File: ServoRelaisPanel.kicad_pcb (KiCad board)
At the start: 2 copper layers, 99.8 x 99.6 mm, 202 parts, among them J1 Conn_01x03_Female, J2 ISCP, J3 Conn_01x02_Female, J4 Conn_01x03_Female, Q1 IRLB8721PBF, Q2 IRLB8721PBF, U1 MEE1-0309, U2 PIC10F320-IP

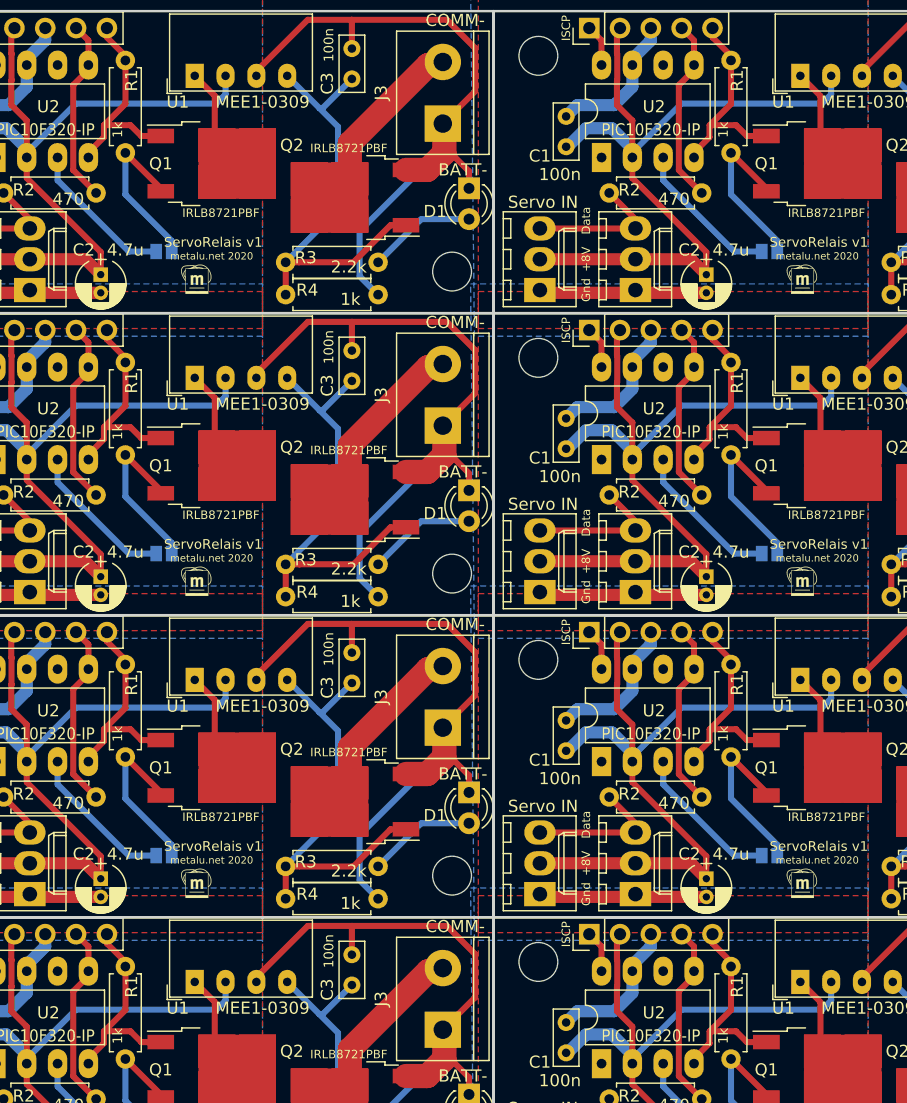
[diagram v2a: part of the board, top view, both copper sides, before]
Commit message: PCB: add solder-switch to disable powering the DC-DC converter (else programming of the PIC fails because of power loss)
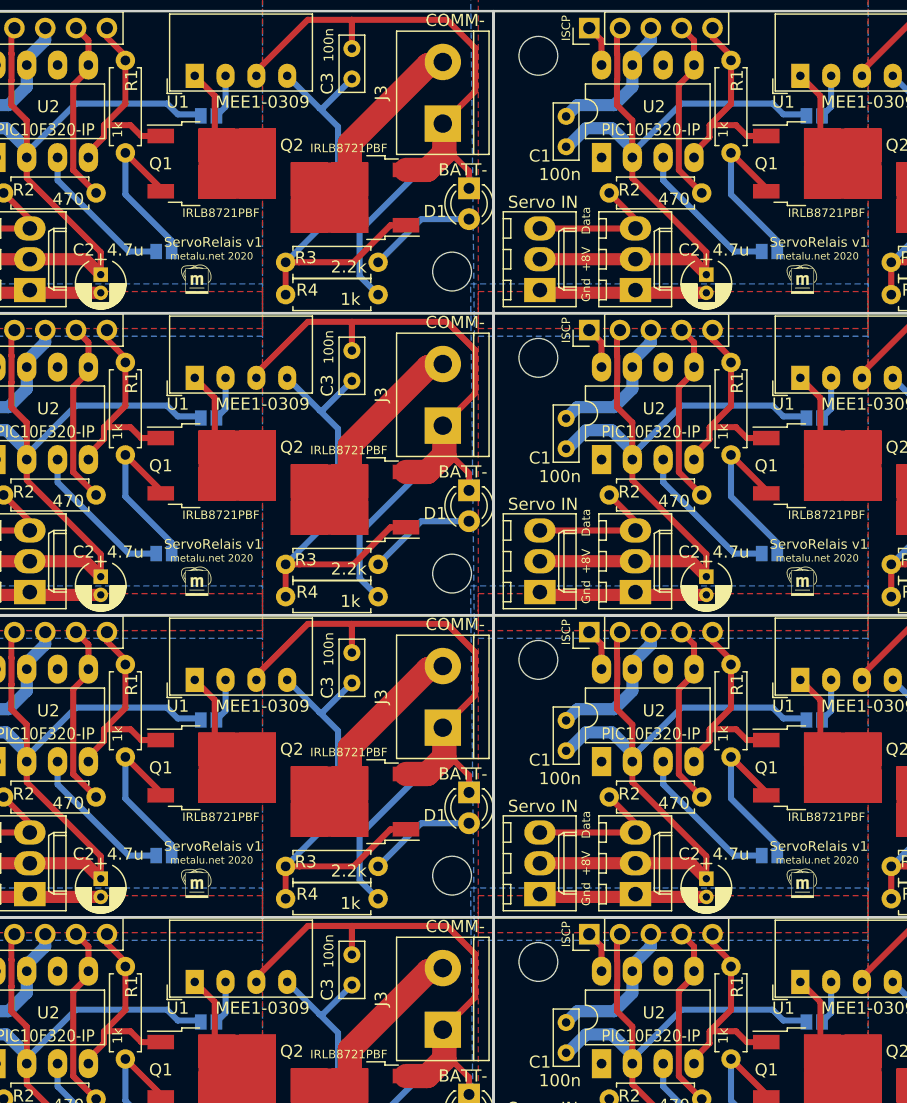
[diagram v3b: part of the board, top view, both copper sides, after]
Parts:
- removed the G*** at (159.1, 127.6)
- removed the G*** at (109.2, 127.6)
- removed the G*** at (159.1, 102.7)
- removed the G*** at (109.2, 102.7)
- removed the G*** at (159.1, 77.9)
- removed the G*** at (109.2, 77.9)
- removed the G*** at (159.1, 53.0)
- added ?: , , F.Cu at (103.9, 143.9)
- added ?: , , F.Cu at (54.0, 143.9)
- added G***: LOGO, metalunet:metalunet, B.Cu at (162.3, 127.4)
- added G***: LOGO, metalunet:metalunet, B.Cu at (112.4, 127.4)
- added G***: LOGO, metalunet:metalunet, B.Cu at (162.3, 102.5)
- added G***: LOGO, metalunet:metalunet, B.Cu at (112.4, 102.5)
- added G***: LOGO, metalunet:metalunet, B.Cu at (162.3, 77.6)
- added G***: LOGO, metalunet:metalunet, B.Cu at (112.4, 77.6)
- added G***: LOGO, metalunet:metalunet, B.Cu at (162.3, 52.7)
- added JP2: (prog), Connect:GS2, B.Cu at (152.7, 123.2)
- added JP2: (prog), Connect:GS2, B.Cu at (102.7, 123.2)
- added JP2: (prog), Connect:GS2, B.Cu at (152.7, 98.3)
- added JP2: (prog), Connect:GS2, B.Cu at (102.7, 98.3)
- added JP2: (prog), Connect:GS2, B.Cu at (152.7, 73.4)
- added JP2: (prog), Connect:GS2, B.Cu at (102.7, 73.4)
- added JP2: (prog), Connect:GS2, B.Cu at (152.7, 48.5)
- added JP2: (prog), Connect:GS2, B.Cu at (102.7, 48.5)
- moved ? 37.0 mm to (127.9, 141.4)
- moved G*** 3.19 mm to (112.4, 52.7)
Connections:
- U1 pad 2: +3V3 -> Net-(JP2-Pad2) (x8)
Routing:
- net Net-(JP2-Pad2): track 0.00 -> 28.9 mm
- net +3V3: track 523.4 -> 495.3 mm

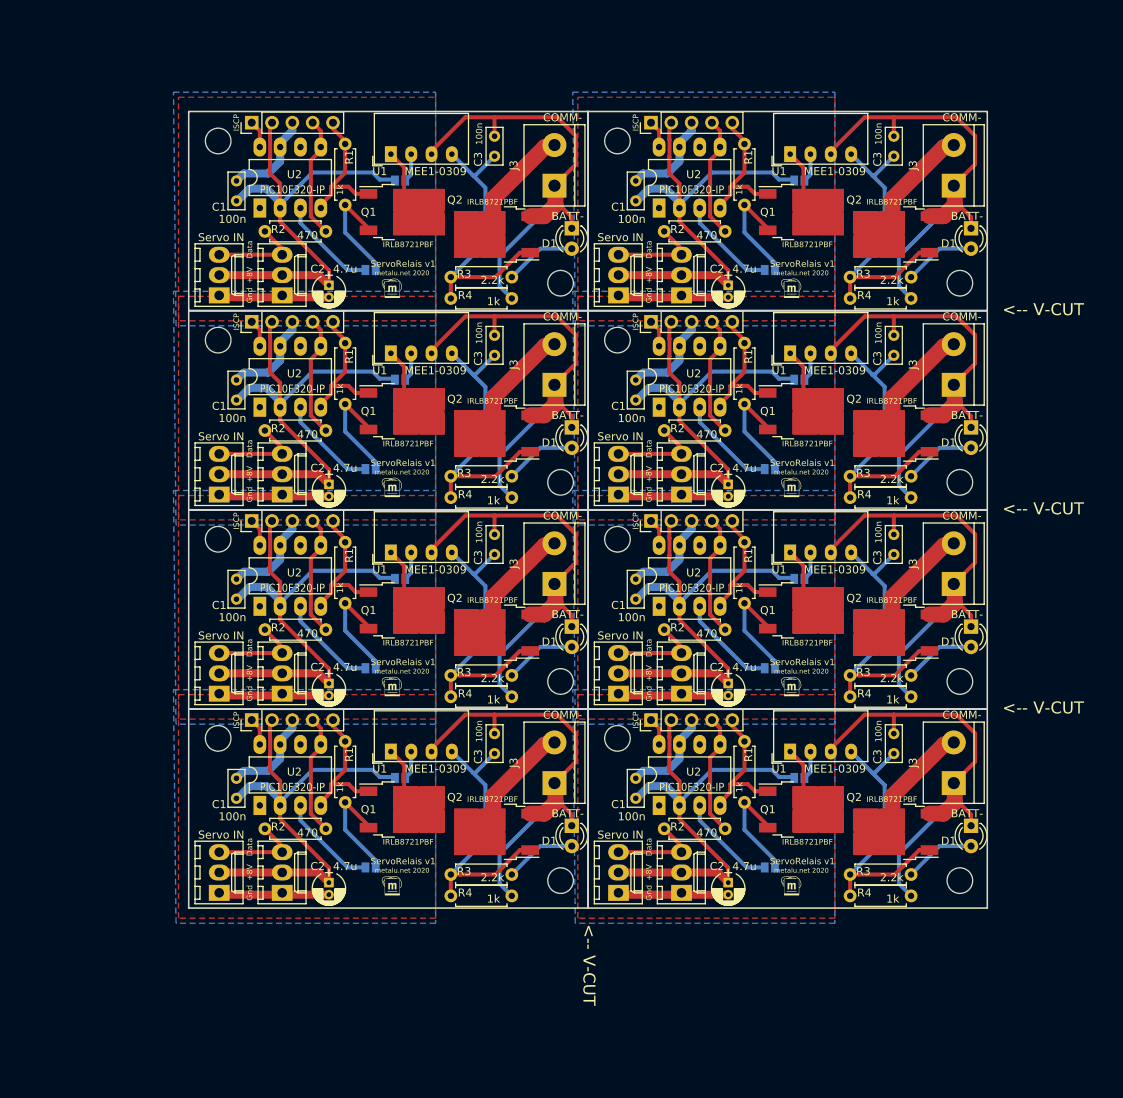
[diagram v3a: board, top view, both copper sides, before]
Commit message: PCB 1.2: add 25Vmax->3V3 regulator
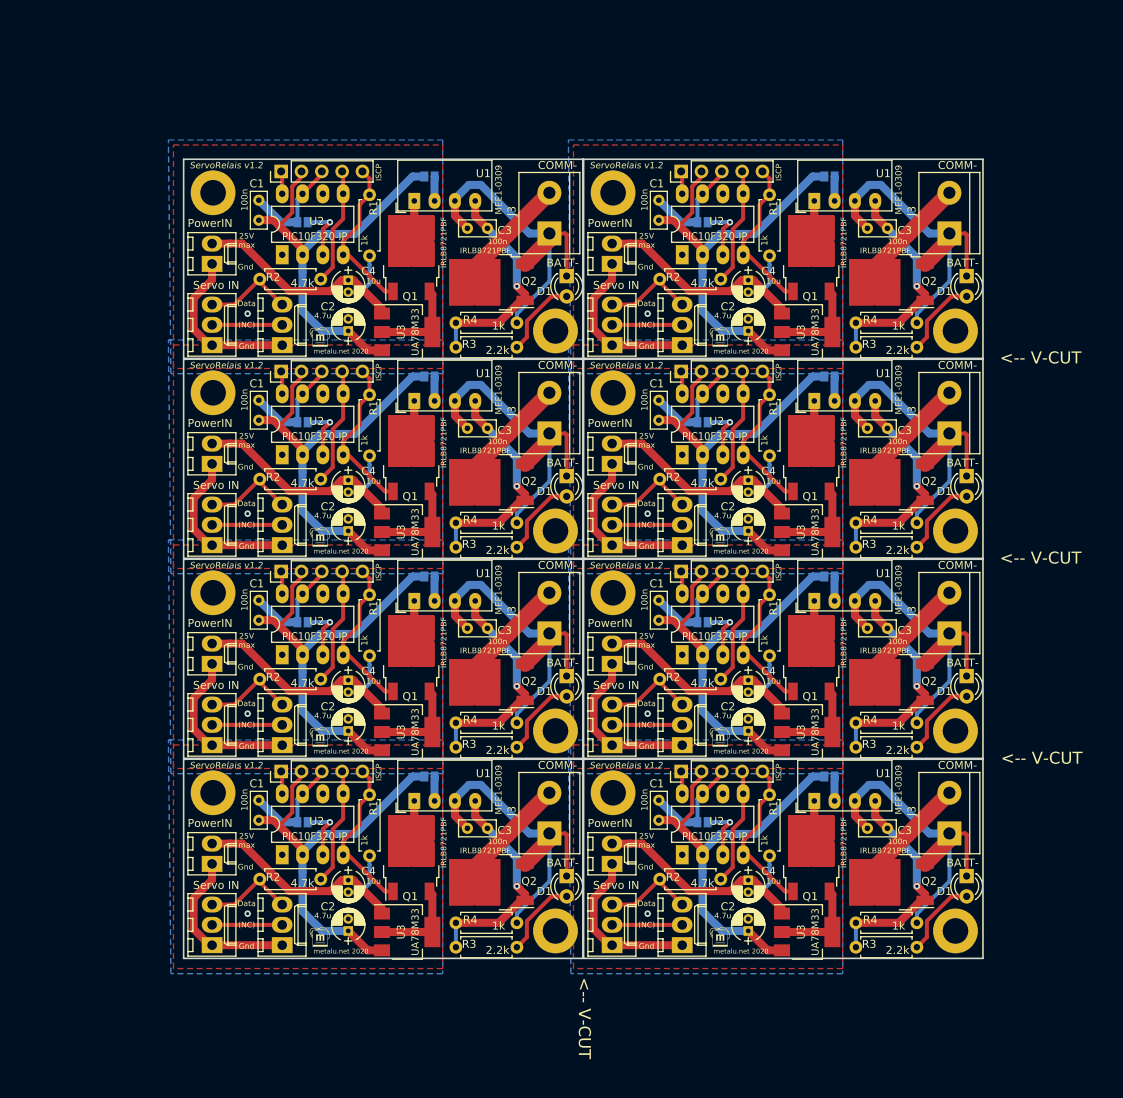
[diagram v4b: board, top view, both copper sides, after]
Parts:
- removed the ? at (139.6, 132.5)
- removed the ? at (140.8, 117.7)
- removed the ? at (90.9, 117.7)
- removed the ? at (140.8, 92.8)
- removed the ? at (90.9, 92.8)
- removed the ? at (140.8, 67.9)
- removed the ? at (140.8, 131.2)
- removed the ? at (90.9, 131.2)
- removed the ? at (140.8, 106.3)
- removed the ? at (90.9, 106.3)
- removed the ? at (140.8, 81.4)
- removed the ? at (89.7, 132.5)
- removed the ? at (90.9, 81.4)
- removed the ? at (140.8, 56.5)
- removed the ? at (139.6, 131.2)
- removed the ? at (89.7, 131.2)
- removed the ? at (139.6, 106.3)
- removed the ? at (89.7, 106.3)
- removed the ? at (139.6, 81.4)
- removed the ? at (89.7, 81.4)
- removed the ? at (139.6, 56.5)
- removed the ? at (140.8, 142.6)
- removed the ? at (139.6, 107.6)
- removed the ? at (127.9, 141.4)
- removed the ? at (90.9, 67.9)
- removed the ? at (89.7, 56.5)
- removed the ? at (90.9, 56.5)
- removed the ? at (89.7, 57.8)
- removed the ? at (89.7, 107.6)
- removed the ? at (139.6, 82.7)
- removed the ? at (89.7, 82.7)
- removed the ? at (139.6, 57.8)
- removed the ? at (103.9, 143.9)
- removed the C1 at (132.2, 125.7)
- removed the C1 at (82.3, 125.7)
- removed the C1 at (132.2, 100.8)
- removed the C1 at (82.3, 100.8)
- removed the C1 at (132.2, 75.9)
- removed the C1 at (82.3, 75.9)
- removed the C1 at (132.2, 51.1)
- removed the C1 at (82.3, 51.1)
- removed the C2 at (143.8, 136.3)
- removed the C2 at (93.9, 136.3)
- removed the C2 at (143.8, 111.4)
- removed the C2 at (93.9, 111.4)
- removed the C2 at (143.8, 86.5)
- removed the C2 at (93.9, 86.5)
- removed the C2 at (143.8, 61.6)
- removed the C3 at (164.5, 120.1)
- removed the C3 at (114.6, 120.1)
- removed the C3 at (164.5, 95.2)
- removed the C3 at (114.6, 95.2)
- removed the C3 at (164.5, 70.4)
- removed the C3 at (114.6, 70.4)
- removed the C3 at (164.5, 45.5)
- removed the C3 at (114.6, 45.5)
- removed the D1 at (174.1, 129.2)
- removed the D1 at (124.2, 129.2)
- removed the D1 at (174.1, 104.3)
- removed the D1 at (124.2, 104.3)
- removed the D1 at (174.1, 79.4)
- removed the D1 at (124.2, 79.4)
- removed the D1 at (174.1, 54.5)
- removed the G*** at (162.3, 127.4)
- removed the G*** at (151.6, 111.8)
- removed the G*** at (101.7, 111.8)
- removed the G*** at (151.6, 86.9)
- removed the G*** at (101.7, 86.9)
- removed the G*** at (151.6, 62.0)
- removed the G*** at (112.4, 127.4)
- removed the G*** at (162.3, 102.5)
- removed the G*** at (112.4, 102.5)
- removed the G*** at (162.3, 77.6)
- removed the G*** at (112.4, 77.6)
- removed the G*** at (162.3, 52.7)
- removed the G*** at (151.6, 136.7)
- removed the G*** at (101.7, 136.7)
- removed the H1 at (129.9, 118.2)
- removed the H1 at (80.0, 118.2)
- removed the H1 at (129.9, 93.3)
- removed the H1 at (80.0, 93.3)
- removed the H1 at (129.9, 68.5)
- removed the H1 at (80.0, 68.5)
- removed the H1 at (129.9, 43.6)
- removed the H2 at (172.7, 136.0)
- removed the H2 at (122.8, 136.0)
- removed the H2 at (172.7, 111.1)
- removed the H2 at (122.8, 111.1)
- removed the H2 at (172.7, 86.2)
- removed the H2 at (122.8, 86.2)
- removed the H2 at (172.7, 61.3)
- removed the J1 at (130.0, 137.5)
- removed the J1 at (80.1, 137.5)
- removed the J1 at (130.0, 112.6)
- removed the J1 at (80.1, 112.6)
- removed the J1 at (130.0, 87.8)
- removed the J1 at (80.1, 87.8)
- removed the J1 at (130.0, 62.9)
- removed the J2 at (134.1, 116.0)
- removed the J2 at (84.2, 116.0)
- removed the J2 at (134.1, 91.1)
- removed the J2 at (84.2, 91.1)
- removed the J2 at (134.1, 66.2)
- removed the J2 at (84.2, 66.2)
- removed the J2 at (134.1, 41.3)
- removed the J3 at (172.0, 123.8)
- removed the J3 at (122.0, 123.8)
- removed the J3 at (172.0, 98.9)
- removed the J3 at (122.0, 98.9)
- removed the J3 at (172.0, 74.0)
- removed the J3 at (122.0, 74.0)
- removed the J3 at (172.0, 49.1)
- removed the J4 at (137.9, 137.5)
- removed the J4 at (88.0, 137.5)
- removed the J4 at (137.9, 112.6)
- removed the J4 at (88.0, 112.6)
- removed the J4 at (137.9, 87.8)
- removed the J4 at (88.0, 87.8)
- removed the J4 at (137.9, 62.9)
- removed the JP1 at (149.0, 134.4)
- removed the JP1 at (99.1, 134.4)
- removed the JP1 at (149.0, 109.5)
- removed the JP1 at (99.1, 109.5)
- removed the JP1 at (149.0, 84.6)
- removed the JP1 at (99.1, 84.6)
- removed the JP1 at (149.0, 59.7)
- removed the JP2 at (152.7, 123.2)
- removed the JP2 at (102.7, 123.2)
- removed the JP2 at (152.7, 98.3)
- removed the JP2 at (102.7, 98.3)
- removed the JP2 at (152.7, 73.4)
- removed the JP2 at (102.7, 73.4)
- removed the JP2 at (152.7, 48.5)
- removed the Q1 at (152.9, 127.1)
- removed the Q1 at (103.0, 127.1)
- removed the Q1 at (152.9, 102.2)
- removed the Q1 at (103.0, 102.2)
- removed the Q1 at (152.9, 77.3)
- removed the Q1 at (103.0, 77.3)
- removed the Q1 at (152.9, 52.5)
- removed the Q1 at (103.0, 52.5)
- removed the Q2 at (164.7, 129.9)
- removed the Q2 at (114.8, 129.9)
- removed the Q2 at (164.7, 105.0)
- removed the Q2 at (114.8, 105.0)
- removed the Q2 at (164.7, 80.1)
- removed the Q2 at (114.8, 80.1)
- removed the Q2 at (164.7, 55.2)
- removed the Q2 at (114.8, 55.2)
- removed the R1 at (145.8, 126.2)
- removed the R1 at (95.9, 126.2)
- removed the R1 at (145.8, 101.3)
- removed the R1 at (95.9, 101.3)
- removed the R1 at (145.8, 76.5)
- removed the R1 at (95.9, 76.5)
- removed the R1 at (145.8, 51.6)
- removed the R2 at (143.4, 129.5)
- removed the R2 at (93.5, 129.5)
- removed the R2 at (143.4, 104.6)
- removed the R2 at (93.5, 104.6)
- removed the R2 at (143.4, 79.8)
- removed the R2 at (93.5, 79.8)
- removed the R2 at (143.4, 54.9)
- removed the R3 at (166.6, 135.3)
- removed the R3 at (116.7, 135.3)
- removed the R3 at (166.6, 110.4)
- removed the R3 at (116.7, 110.4)
- removed the R3 at (166.6, 85.5)
- removed the R3 at (116.7, 85.5)
- removed the R3 at (166.6, 60.6)
- removed the R4 at (166.6, 137.9)
- removed the R4 at (116.7, 137.9)
- removed the R4 at (166.6, 113.0)
- removed the R4 at (116.7, 113.0)
- removed the R4 at (166.6, 88.1)
- removed the R4 at (116.7, 88.1)
- removed the R4 at (166.6, 63.2)
- removed the U1 at (151.5, 119.9)
- removed the U1 at (101.6, 119.9)
- removed the U1 at (151.5, 95.0)
- removed the U1 at (101.6, 95.0)
- removed the U1 at (151.5, 70.1)
- removed the U1 at (101.6, 70.1)
- removed the U1 at (151.5, 45.2)
- removed the U2 at (135.1, 126.6)
- removed the U2 at (85.2, 126.6)
- removed the U2 at (135.1, 101.7)
- removed the U2 at (85.2, 101.7)
- removed the U2 at (135.1, 76.8)
- removed the U2 at (85.2, 76.8)
- removed the U2 at (135.1, 51.9)
- added ?: , , F.Cu at (140.3, 137.5)
- added ?: , , F.Cu at (140.3, 123.9)
- added ?: , , F.Cu at (90.3, 123.9)
- added ?: , , F.Cu at (140.3, 98.9)
- added ?: , , F.Cu at (90.3, 98.9)
- added ?: , , F.Cu at (140.3, 73.9)
- added ?: , , F.Cu at (139.0, 137.5)
- added ?: , , F.Cu at (89.0, 137.5)
- added ?: , , F.Cu at (139.0, 112.5)
- added ?: , , F.Cu at (89.0, 112.5)
- added ?: , , F.Cu at (139.0, 87.5)
- added ?: , , F.Cu at (90.3, 137.5)
- added ?: , , F.Cu at (89.0, 87.5)
- added ?: , , F.Cu at (139.0, 62.5)
- added ?: , , F.Cu at (139.0, 138.8)
- added ?: , , F.Cu at (89.0, 138.8)
- added ?: , , F.Cu at (139.0, 113.8)
- added ?: , , F.Cu at (89.0, 113.8)
- added ?: , , F.Cu at (139.0, 88.8)
- added ?: , , F.Cu at (89.0, 88.8)
- added ?: , , F.Cu at (139.0, 63.8)
- added ?: , , F.Cu at (140.3, 112.5)
- added ?: , , F.Cu at (90.3, 73.9)
- added ?: , , F.Cu at (89.0, 62.5)
- added ?: , , F.Cu at (90.3, 62.5)
- added ?: , , F.Cu at (89.0, 63.8)
- added ?: , , F.Cu at (90.3, 112.5)
- added ?: , , F.Cu at (140.3, 87.5)
- added ?: , , F.Cu at (90.3, 87.5)
- added ?: , , F.Cu at (140.3, 62.5)
- added ?: , , F.Cu at (140.3, 148.9)
- added ?: , , F.Cu at (90.3, 148.9)
- added C1: 100n, Capacitors_ThroughHole:C_Rect_L4.6mm_W2.0mm_P2.50mm_MKS02_FKP02, F.Cu at (135.1, 128.5)
- added C1: 100n, Capacitors_ThroughHole:C_Rect_L4.6mm_W2.0mm_P2.50mm_MKS02_FKP02, F.Cu at (85.1, 128.5)
- added C1: 100n, Capacitors_ThroughHole:C_Rect_L4.6mm_W2.0mm_P2.50mm_MKS02_FKP02, F.Cu at (135.1, 103.5)
- added C1: 100n, Capacitors_ThroughHole:C_Rect_L4.6mm_W2.0mm_P2.50mm_MKS02_FKP02, F.Cu at (85.1, 103.5)
- added C1: 100n, Capacitors_ThroughHole:C_Rect_L4.6mm_W2.0mm_P2.50mm_MKS02_FKP02, F.Cu at (135.1, 78.5)
- added C1: 100n, Capacitors_ThroughHole:C_Rect_L4.6mm_W2.0mm_P2.50mm_MKS02_FKP02, F.Cu at (85.1, 78.5)
- added C1: 100n, Capacitors_ThroughHole:C_Rect_L4.6mm_W2.0mm_P2.50mm_MKS02_FKP02, F.Cu at (135.1, 53.5)
- added C1: 100n, Capacitors_ThroughHole:C_Rect_L4.6mm_W2.0mm_P2.50mm_MKS02_FKP02, F.Cu at (85.1, 53.5)
- added C2: 4.7u, Capacitors_ThroughHole:CP_Radial_D4.0mm_P1.50mm, F.Cu at (146.3, 142.3)
- added C2: 4.7u, Capacitors_ThroughHole:CP_Radial_D4.0mm_P1.50mm, F.Cu at (96.3, 142.3)
- added C2: 4.7u, Capacitors_ThroughHole:CP_Radial_D4.0mm_P1.50mm, F.Cu at (146.3, 117.3)
- added C2: 4.7u, Capacitors_ThroughHole:CP_Radial_D4.0mm_P1.50mm, F.Cu at (96.3, 117.3)
- added C2: 4.7u, Capacitors_ThroughHole:CP_Radial_D4.0mm_P1.50mm, F.Cu at (146.3, 92.3)
- added C2: 4.7u, Capacitors_ThroughHole:CP_Radial_D4.0mm_P1.50mm, F.Cu at (96.3, 92.3)
- added C2: 4.7u, Capacitors_ThroughHole:CP_Radial_D4.0mm_P1.50mm, F.Cu at (146.3, 67.3)
- added C3: 100n, Capacitors_ThroughHole:C_Rect_L4.6mm_W2.0mm_P2.50mm_MKS02_FKP02, F.Cu at (163.7, 129.5)
- added C3: 100n, Capacitors_ThroughHole:C_Rect_L4.6mm_W2.0mm_P2.50mm_MKS02_FKP02, F.Cu at (113.7, 129.5)
- added C3: 100n, Capacitors_ThroughHole:C_Rect_L4.6mm_W2.0mm_P2.50mm_MKS02_FKP02, F.Cu at (163.7, 104.5)
- added C3: 100n, Capacitors_ThroughHole:C_Rect_L4.6mm_W2.0mm_P2.50mm_MKS02_FKP02, F.Cu at (113.7, 104.5)
- added C3: 100n, Capacitors_ThroughHole:C_Rect_L4.6mm_W2.0mm_P2.50mm_MKS02_FKP02, F.Cu at (163.7, 79.5)
- added C3: 100n, Capacitors_ThroughHole:C_Rect_L4.6mm_W2.0mm_P2.50mm_MKS02_FKP02, F.Cu at (113.7, 79.5)
- added C3: 100n, Capacitors_ThroughHole:C_Rect_L4.6mm_W2.0mm_P2.50mm_MKS02_FKP02, F.Cu at (163.7, 54.5)
- added C3: 100n, Capacitors_ThroughHole:C_Rect_L4.6mm_W2.0mm_P2.50mm_MKS02_FKP02, F.Cu at (113.7, 54.5)
- added C4: 10u, Capacitors_ThroughHole:CP_Radial_D4.0mm_P1.50mm, F.Cu at (146.3, 136.0)
- added C4: 10u, Capacitors_ThroughHole:CP_Radial_D4.0mm_P1.50mm, F.Cu at (96.3, 136.0)
- added C4: 10u, Capacitors_ThroughHole:CP_Radial_D4.0mm_P1.50mm, F.Cu at (146.3, 111.0)
- added C4: 10u, Capacitors_ThroughHole:CP_Radial_D4.0mm_P1.50mm, F.Cu at (96.3, 111.0)
- added C4: 10u, Capacitors_ThroughHole:CP_Radial_D4.0mm_P1.50mm, F.Cu at (146.3, 86.0)
- added C4: 10u, Capacitors_ThroughHole:CP_Radial_D4.0mm_P1.50mm, F.Cu at (96.3, 86.0)
- added C4: 10u, Capacitors_ThroughHole:CP_Radial_D4.0mm_P1.50mm, F.Cu at (146.3, 61.0)
- added C4: 10u, Capacitors_ThroughHole:CP_Radial_D4.0mm_P1.50mm, F.Cu at (96.3, 61.0)
- added D1: LED, LEDs:LED_D3.0mm, F.Cu at (173.6, 135.5)
- added D1: LED, LEDs:LED_D3.0mm, F.Cu at (123.6, 135.5)
- added D1: LED, LEDs:LED_D3.0mm, F.Cu at (173.6, 110.5)
- added D1: LED, LEDs:LED_D3.0mm, F.Cu at (123.6, 110.5)
- added D1: LED, LEDs:LED_D3.0mm, F.Cu at (173.6, 85.5)
- added D1: LED, LEDs:LED_D3.0mm, F.Cu at (123.6, 85.5)
- added D1: LED, LEDs:LED_D3.0mm, F.Cu at (173.6, 60.5)
- added G***: LOGO, metalunet:metalunet, B.Cu at (156.8, 137.5)
- added G***: LOGO, metalunet:metalunet-mini, F.Cu at (142.7, 118.1)
- added G***: LOGO, metalunet:metalunet-mini, F.Cu at (92.7, 118.1)
- added G***: LOGO, metalunet:metalunet-mini, F.Cu at (142.7, 93.1)
- added G***: LOGO, metalunet:metalunet-mini, F.Cu at (92.7, 93.1)
- added G***: LOGO, metalunet:metalunet-mini, F.Cu at (142.7, 68.1)
- added G***: LOGO, metalunet:metalunet, B.Cu at (106.8, 137.5)
- added G***: LOGO, metalunet:metalunet, B.Cu at (156.8, 112.5)
- added G***: LOGO, metalunet:metalunet, B.Cu at (106.8, 112.5)
- added G***: LOGO, metalunet:metalunet, B.Cu at (156.8, 87.5)
- added G***: LOGO, metalunet:metalunet, B.Cu at (106.8, 87.5)
- added G***: LOGO, metalunet:metalunet, B.Cu at (156.8, 62.5)
- added G***: LOGO, metalunet:metalunet-mini, F.Cu at (142.7, 143.1)
- added G***: LOGO, metalunet:metalunet-mini, F.Cu at (92.7, 143.1)
- added H1: MountingHole, Mounting_Holes:MountingHole_3.2mm_M3_DIN965_Pad, F.Cu at (129.4, 125.0)
- added H1: MountingHole, Mounting_Holes:MountingHole_3.2mm_M3_DIN965_Pad, F.Cu at (79.4, 125.0)
- added H1: MountingHole, Mounting_Holes:MountingHole_3.2mm_M3_DIN965_Pad, F.Cu at (129.4, 100.0)
- added H1: MountingHole, Mounting_Holes:MountingHole_3.2mm_M3_DIN965_Pad, F.Cu at (79.4, 100.0)
- added H1: MountingHole, Mounting_Holes:MountingHole_3.2mm_M3_DIN965_Pad, F.Cu at (129.4, 75.0)
- added H1: MountingHole, Mounting_Holes:MountingHole_3.2mm_M3_DIN965_Pad, F.Cu at (79.4, 75.0)
- added H1: MountingHole, Mounting_Holes:MountingHole_3.2mm_M3_DIN965_Pad, F.Cu at (129.4, 50.0)
- added H2: MountingHole, Mounting_Holes:MountingHole_3.2mm_M3_DIN965_Pad, F.Cu at (172.2, 142.3)
- added H2: MountingHole, Mounting_Holes:MountingHole_3.2mm_M3_DIN965_Pad, F.Cu at (122.2, 142.3)
- added H2: MountingHole, Mounting_Holes:MountingHole_3.2mm_M3_DIN965_Pad, F.Cu at (172.2, 117.3)
- added H2: MountingHole, Mounting_Holes:MountingHole_3.2mm_M3_DIN965_Pad, F.Cu at (122.2, 117.3)
- added H2: MountingHole, Mounting_Holes:MountingHole_3.2mm_M3_DIN965_Pad, F.Cu at (172.2, 92.3)
- added H2: MountingHole, Mounting_Holes:MountingHole_3.2mm_M3_DIN965_Pad, F.Cu at (122.2, 92.3)
- added H2: MountingHole, Mounting_Holes:MountingHole_3.2mm_M3_DIN965_Pad, F.Cu at (172.2, 67.3)
- added J1: Servo, Connectors_Molex:Molex_KK-6410-03_03x2.54mm_Straight, F.Cu at (129.2, 144.1)
- added J1: Servo, Connectors_Molex:Molex_KK-6410-03_03x2.54mm_Straight, F.Cu at (79.2, 144.1)
- added J1: Servo, Connectors_Molex:Molex_KK-6410-03_03x2.54mm_Straight, F.Cu at (129.2, 119.1)
- added J1: Servo, Connectors_Molex:Molex_KK-6410-03_03x2.54mm_Straight, F.Cu at (79.2, 119.1)
- added J1: Servo, Connectors_Molex:Molex_KK-6410-03_03x2.54mm_Straight, F.Cu at (129.2, 94.1)
- added J1: Servo, Connectors_Molex:Molex_KK-6410-03_03x2.54mm_Straight, F.Cu at (79.2, 94.1)
- added J1: Servo, Connectors_Molex:Molex_KK-6410-03_03x2.54mm_Straight, F.Cu at (129.2, 69.1)
- added J2: ISCP, Pin_Headers:Pin_Header_Straight_1x05_Pitch2.54mm, F.Cu at (137.9, 122.4)
- added J2: ISCP, Pin_Headers:Pin_Header_Straight_1x05_Pitch2.54mm, F.Cu at (87.9, 122.4)
- added J2: ISCP, Pin_Headers:Pin_Header_Straight_1x05_Pitch2.54mm, F.Cu at (137.9, 97.4)
- added J2: ISCP, Pin_Headers:Pin_Header_Straight_1x05_Pitch2.54mm, F.Cu at (87.9, 97.4)
- added J2: ISCP, Pin_Headers:Pin_Header_Straight_1x05_Pitch2.54mm, F.Cu at (137.9, 72.4)
- added J2: ISCP, Pin_Headers:Pin_Header_Straight_1x05_Pitch2.54mm, F.Cu at (87.9, 72.4)
- added J2: ISCP, Pin_Headers:Pin_Header_Straight_1x05_Pitch2.54mm, F.Cu at (137.9, 47.4)
- added J3: Bornier, Terminal_Blocks:TerminalBlock_bornier-2_P5.08mm, F.Cu at (171.4, 130.1)
- added J3: Bornier, Terminal_Blocks:TerminalBlock_bornier-2_P5.08mm, F.Cu at (121.4, 130.1)
- added J3: Bornier, Terminal_Blocks:TerminalBlock_bornier-2_P5.08mm, F.Cu at (171.4, 105.1)
- added J3: Bornier, Terminal_Blocks:TerminalBlock_bornier-2_P5.08mm, F.Cu at (121.4, 105.1)
- added J3: Bornier, Terminal_Blocks:TerminalBlock_bornier-2_P5.08mm, F.Cu at (171.4, 80.1)
- added J3: Bornier, Terminal_Blocks:TerminalBlock_bornier-2_P5.08mm, F.Cu at (121.4, 80.1)
- added J3: Bornier, Terminal_Blocks:TerminalBlock_bornier-2_P5.08mm, F.Cu at (171.4, 55.1)
- added J4: Servo, Connectors_Molex:Molex_KK-6410-03_03x2.54mm_Straight, F.Cu at (138.0, 144.1)
- added J4: Servo, Connectors_Molex:Molex_KK-6410-03_03x2.54mm_Straight, F.Cu at (88.0, 144.1)
- added J4: Servo, Connectors_Molex:Molex_KK-6410-03_03x2.54mm_Straight, F.Cu at (138.0, 119.1)
- added J4: Servo, Connectors_Molex:Molex_KK-6410-03_03x2.54mm_Straight, F.Cu at (88.0, 119.1)
- added J4: Servo, Connectors_Molex:Molex_KK-6410-03_03x2.54mm_Straight, F.Cu at (138.0, 94.1)
- added J4: Servo, Connectors_Molex:Molex_KK-6410-03_03x2.54mm_Straight, F.Cu at (88.0, 94.1)
- added J4: Servo, Connectors_Molex:Molex_KK-6410-03_03x2.54mm_Straight, F.Cu at (138.0, 69.1)
- added J5: PowerIN, Connectors_Molex:Molex_KK-6410-02_02x2.54mm_Straight, F.Cu at (129.2, 133.9)
- added J5: PowerIN, Connectors_Molex:Molex_KK-6410-02_02x2.54mm_Straight, F.Cu at (79.2, 133.9)
- added J5: PowerIN, Connectors_Molex:Molex_KK-6410-02_02x2.54mm_Straight, F.Cu at (129.2, 108.9)
- added J5: PowerIN, Connectors_Molex:Molex_KK-6410-02_02x2.54mm_Straight, F.Cu at (79.2, 108.9)
- added J5: PowerIN, Connectors_Molex:Molex_KK-6410-02_02x2.54mm_Straight, F.Cu at (129.2, 83.9)
- added J5: PowerIN, Connectors_Molex:Molex_KK-6410-02_02x2.54mm_Straight, F.Cu at (79.2, 83.9)
- added J5: PowerIN, Connectors_Molex:Molex_KK-6410-02_02x2.54mm_Straight, F.Cu at (129.2, 58.9)
- added J5: PowerIN, Connectors_Molex:Molex_KK-6410-02_02x2.54mm_Straight, F.Cu at (79.2, 58.9)
- added JP1: Config, Connect:GS2, B.Cu at (140.6, 128.7)
- added JP1: Config, Connect:GS2, B.Cu at (90.6, 128.7)
- added JP1: Config, Connect:GS2, B.Cu at (140.6, 103.7)
- added JP1: Config, Connect:GS2, B.Cu at (90.6, 103.7)
- added JP1: Config, Connect:GS2, B.Cu at (140.6, 78.7)
- added JP1: Config, Connect:GS2, B.Cu at (90.6, 78.7)
- added JP1: Config, Connect:GS2, B.Cu at (140.6, 53.7)
- added JP2: (prog), Connect:GS2, B.Cu at (156.4, 123.0)
- added JP2: (prog), Connect:GS2, B.Cu at (106.4, 123.0)
- added JP2: (prog), Connect:GS2, B.Cu at (156.4, 98.0)
- added JP2: (prog), Connect:GS2, B.Cu at (106.4, 98.0)
- added JP2: (prog), Connect:GS2, B.Cu at (156.4, 73.0)
- added JP2: (prog), Connect:GS2, B.Cu at (106.4, 73.0)
- added JP2: (prog), Connect:GS2, B.Cu at (156.4, 48.0)
- added Q1: IRLB8721PBF, TO_SOT_Packages_SMD:TO-252-2, F.Cu at (154.1, 133.2)
- added Q1: IRLB8721PBF, TO_SOT_Packages_SMD:TO-252-2, F.Cu at (104.1, 133.2)
- added Q1: IRLB8721PBF, TO_SOT_Packages_SMD:TO-252-2, F.Cu at (154.1, 108.2)
- added Q1: IRLB8721PBF, TO_SOT_Packages_SMD:TO-252-2, F.Cu at (104.1, 108.2)
- added Q1: IRLB8721PBF, TO_SOT_Packages_SMD:TO-252-2, F.Cu at (154.1, 83.2)
- added Q1: IRLB8721PBF, TO_SOT_Packages_SMD:TO-252-2, F.Cu at (104.1, 83.2)
- added Q1: IRLB8721PBF, TO_SOT_Packages_SMD:TO-252-2, F.Cu at (154.1, 58.2)
- added Q1: IRLB8721PBF, TO_SOT_Packages_SMD:TO-252-2, F.Cu at (104.1, 58.2)
- added Q2: IRLB8721PBF, TO_SOT_Packages_SMD:TO-252-2, F.Cu at (164.2, 136.2)
- added Q2: IRLB8721PBF, TO_SOT_Packages_SMD:TO-252-2, F.Cu at (114.2, 136.2)
- added Q2: IRLB8721PBF, TO_SOT_Packages_SMD:TO-252-2, F.Cu at (164.2, 111.2)
- added Q2: IRLB8721PBF, TO_SOT_Packages_SMD:TO-252-2, F.Cu at (114.2, 111.2)
- added Q2: IRLB8721PBF, TO_SOT_Packages_SMD:TO-252-2, F.Cu at (164.2, 86.2)
- added Q2: IRLB8721PBF, TO_SOT_Packages_SMD:TO-252-2, F.Cu at (114.2, 86.2)
- added Q2: IRLB8721PBF, TO_SOT_Packages_SMD:TO-252-2, F.Cu at (164.2, 61.2)
- added Q2: IRLB8721PBF, TO_SOT_Packages_SMD:TO-252-2, F.Cu at (114.2, 61.2)
- added R1: 1k, Resistors_ThroughHole:R_Axial_DIN0207_L6.3mm_D2.5mm_P7.62mm_Horizontal, F.Cu at (148.9, 132.9)
- added R1: 1k, Resistors_ThroughHole:R_Axial_DIN0207_L6.3mm_D2.5mm_P7.62mm_Horizontal, F.Cu at (98.9, 132.9)
- added R1: 1k, Resistors_ThroughHole:R_Axial_DIN0207_L6.3mm_D2.5mm_P7.62mm_Horizontal, F.Cu at (148.9, 107.9)
- added R1: 1k, Resistors_ThroughHole:R_Axial_DIN0207_L6.3mm_D2.5mm_P7.62mm_Horizontal, F.Cu at (98.9, 107.9)
- added R1: 1k, Resistors_ThroughHole:R_Axial_DIN0207_L6.3mm_D2.5mm_P7.62mm_Horizontal, F.Cu at (148.9, 82.9)
- added R1: 1k, Resistors_ThroughHole:R_Axial_DIN0207_L6.3mm_D2.5mm_P7.62mm_Horizontal, F.Cu at (98.9, 82.9)
- added R1: 1k, Resistors_ThroughHole:R_Axial_DIN0207_L6.3mm_D2.5mm_P7.62mm_Horizontal, F.Cu at (148.9, 57.9)
- added R2: 4.7k, Resistors_ThroughHole:R_Axial_DIN0207_L6.3mm_D2.5mm_P7.62mm_Horizontal, F.Cu at (142.8, 135.8)
- added R2: 4.7k, Resistors_ThroughHole:R_Axial_DIN0207_L6.3mm_D2.5mm_P7.62mm_Horizontal, F.Cu at (92.8, 135.8)
- added R2: 4.7k, Resistors_ThroughHole:R_Axial_DIN0207_L6.3mm_D2.5mm_P7.62mm_Horizontal, F.Cu at (142.8, 110.8)
- added R2: 4.7k, Resistors_ThroughHole:R_Axial_DIN0207_L6.3mm_D2.5mm_P7.62mm_Horizontal, F.Cu at (92.8, 110.8)
- added R2: 4.7k, Resistors_ThroughHole:R_Axial_DIN0207_L6.3mm_D2.5mm_P7.62mm_Horizontal, F.Cu at (142.8, 85.8)
- added R2: 4.7k, Resistors_ThroughHole:R_Axial_DIN0207_L6.3mm_D2.5mm_P7.62mm_Horizontal, F.Cu at (92.8, 85.8)
- added R2: 4.7k, Resistors_ThroughHole:R_Axial_DIN0207_L6.3mm_D2.5mm_P7.62mm_Horizontal, F.Cu at (142.8, 60.8)
- added R3: 2.2k, Resistors_ThroughHole:R_Axial_DIN0207_L6.3mm_D2.5mm_P7.62mm_Horizontal, F.Cu at (167.3, 144.3)
- added R3: 2.2k, Resistors_ThroughHole:R_Axial_DIN0207_L6.3mm_D2.5mm_P7.62mm_Horizontal, F.Cu at (117.3, 144.3)
- added R3: 2.2k, Resistors_ThroughHole:R_Axial_DIN0207_L6.3mm_D2.5mm_P7.62mm_Horizontal, F.Cu at (167.3, 119.3)
- added R3: 2.2k, Resistors_ThroughHole:R_Axial_DIN0207_L6.3mm_D2.5mm_P7.62mm_Horizontal, F.Cu at (117.3, 119.3)
- added R3: 2.2k, Resistors_ThroughHole:R_Axial_DIN0207_L6.3mm_D2.5mm_P7.62mm_Horizontal, F.Cu at (167.3, 94.3)
- added R3: 2.2k, Resistors_ThroughHole:R_Axial_DIN0207_L6.3mm_D2.5mm_P7.62mm_Horizontal, F.Cu at (117.3, 94.3)
- added R3: 2.2k, Resistors_ThroughHole:R_Axial_DIN0207_L6.3mm_D2.5mm_P7.62mm_Horizontal, F.Cu at (167.3, 69.3)
- added R4: 1k, Resistors_ThroughHole:R_Axial_DIN0207_L6.3mm_D2.5mm_P7.62mm_Horizontal, F.Cu at (167.3, 141.3)
- added R4: 1k, Resistors_ThroughHole:R_Axial_DIN0207_L6.3mm_D2.5mm_P7.62mm_Horizontal, F.Cu at (117.3, 141.3)
- added R4: 1k, Resistors_ThroughHole:R_Axial_DIN0207_L6.3mm_D2.5mm_P7.62mm_Horizontal, F.Cu at (167.3, 116.3)
- added R4: 1k, Resistors_ThroughHole:R_Axial_DIN0207_L6.3mm_D2.5mm_P7.62mm_Horizontal, F.Cu at (117.3, 116.3)
- added R4: 1k, Resistors_ThroughHole:R_Axial_DIN0207_L6.3mm_D2.5mm_P7.62mm_Horizontal, F.Cu at (167.3, 91.3)
- added R4: 1k, Resistors_ThroughHole:R_Axial_DIN0207_L6.3mm_D2.5mm_P7.62mm_Horizontal, F.Cu at (117.3, 91.3)
- added R4: 1k, Resistors_ThroughHole:R_Axial_DIN0207_L6.3mm_D2.5mm_P7.62mm_Horizontal, F.Cu at (167.3, 66.3)
- added U1: MEE1-0309, Converters_DCDC_ACDC:DCDC-Conv_muRata_CRE1xxxxxxSC, F.Cu at (154.5, 126.1)
- added U1: MEE1-0309, Converters_DCDC_ACDC:DCDC-Conv_muRata_CRE1xxxxxxSC, F.Cu at (104.5, 126.1)
- added U1: MEE1-0309, Converters_DCDC_ACDC:DCDC-Conv_muRata_CRE1xxxxxxSC, F.Cu at (154.5, 101.1)
- added U1: MEE1-0309, Converters_DCDC_ACDC:DCDC-Conv_muRata_CRE1xxxxxxSC, F.Cu at (104.5, 101.1)
- added U1: MEE1-0309, Converters_DCDC_ACDC:DCDC-Conv_muRata_CRE1xxxxxxSC, F.Cu at (154.5, 76.1)
- added U1: MEE1-0309, Converters_DCDC_ACDC:DCDC-Conv_muRata_CRE1xxxxxxSC, F.Cu at (104.5, 76.1)
- added U1: MEE1-0309, Converters_DCDC_ACDC:DCDC-Conv_muRata_CRE1xxxxxxSC, F.Cu at (154.5, 51.1)
- added U2: PIC10F320-IP, Housings_DIP:DIP-8_W7.62mm_LongPads, F.Cu at (138.0, 132.8)
- added U2: PIC10F320-IP, Housings_DIP:DIP-8_W7.62mm_LongPads, F.Cu at (88.0, 132.8)
- added U2: PIC10F320-IP, Housings_DIP:DIP-8_W7.62mm_LongPads, F.Cu at (138.0, 107.8)
- added U2: PIC10F320-IP, Housings_DIP:DIP-8_W7.62mm_LongPads, F.Cu at (88.0, 107.8)
- added U2: PIC10F320-IP, Housings_DIP:DIP-8_W7.62mm_LongPads, F.Cu at (138.0, 82.8)
- added U2: PIC10F320-IP, Housings_DIP:DIP-8_W7.62mm_LongPads, F.Cu at (88.0, 82.8)
- added U2: PIC10F320-IP, Housings_DIP:DIP-8_W7.62mm_LongPads, F.Cu at (138.0, 57.8)
- added U3: UA78M33, TO_SOT_Packages_SMD:SOT-223-3_TabPin2, F.Cu at (153.6, 142.4)
- added U3: UA78M33, TO_SOT_Packages_SMD:SOT-223-3_TabPin2, F.Cu at (103.6, 142.4)
- added U3: UA78M33, TO_SOT_Packages_SMD:SOT-223-3_TabPin2, F.Cu at (153.6, 117.4)
- added U3: UA78M33, TO_SOT_Packages_SMD:SOT-223-3_TabPin2, F.Cu at (103.6, 117.4)
- added U3: UA78M33, TO_SOT_Packages_SMD:SOT-223-3_TabPin2, F.Cu at (153.6, 92.4)
- added U3: UA78M33, TO_SOT_Packages_SMD:SOT-223-3_TabPin2, F.Cu at (103.6, 92.4)
- added U3: UA78M33, TO_SOT_Packages_SMD:SOT-223-3_TabPin2, F.Cu at (153.6, 67.4)
- added U3: UA78M33, TO_SOT_Packages_SMD:SOT-223-3_TabPin2, F.Cu at (103.6, 67.4)
- H1, H2: footprint Mounting_Holes:MountingHole_3.2mm_M3 -> Mounting_Holes:MountingHole_3.2mm_M3_DIN965_Pad
- J1, J4: value Conn_01x03_Female -> Servo
- J3: value Conn_01x02_Female -> Bornier
- R2: value 470 -> 4.7k
- moved G*** 11.3 mm to (106.8, 62.5)
- moved G*** 10.9 mm to (92.7, 68.1)
- moved JP1 10.4 mm to (90.6, 53.7), turned to 90 degrees
- moved R3 8.79 mm to (117.3, 69.3)
- moved J2 7.12 mm to (87.9, 47.4)
- moved R1 7.04 mm to (98.9, 57.9)
- moved U1 6.53 mm to (104.5, 51.1)
- moved H1 6.51 mm to (79.4, 50.0)
- moved U2 6.48 mm to (88.0, 57.8)
- moved J1 6.29 mm to (79.2, 69.1)
- moved J4 6.22 mm to (88.0, 69.1)
- moved C2 6.20 mm to (96.3, 67.3), turned to 90 degrees
- moved D1 6.00 mm to (123.6, 60.5)
- moved H2 6.00 mm to (122.2, 67.3)
- moved J3 6.00 mm to (121.4, 55.1)
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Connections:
- J1 pad 2: +3V3 -> Net-(J1-Pad2)
- J4 pad 2: +3V3 -> Net-(J1-Pad2)
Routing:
- net Net-(C4-Pad1): track 0.00 -> 210.8 mm
- net GNDPWR: track 467.0 -> 357.7 mm
- net GND: track 318.7 -> 421.6 mm, vias 0 -> 8
- net Net-(J1-Pad2): track 0.00 -> 70.1 mm
- net Net-(C3-Pad1): track 291.2 -> 223.0 mm, vias 0 -> 8
- net +3V3: track 495.3 -> 433.1 mm
- net Net-(JP1-Pad1): track 99.5 -> 57.8 mm, vias 0 -> 8
- net Net-(Q1-Pad2): track 69.5 -> 41.4 mm
- net /PGC: track 140.5 -> 162.2 mm
- net Net-(J3-Pad2): track 107.3 -> 120.4 mm
- net Net-(D1-Pad2): track 71.7 -> 80.3 mm
- net /PGD: track 122.5 -> 117.4 mm
- net /Vpp: track 27.8 -> 22.8 mm
- net Net-(JP2-Pad2): track 28.9 -> 24.4 mm
- net Net-(J1-Pad3): track 93.5 -> 92.9 mm
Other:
- board size 99.8 x 99.6 mm -> 99.9 x 99.9 mm
- board text added: "(NC)"
- board text added: "25V max"
- board text added: "ServoRelais v1.2"
- board text added: "ServoRelais v1.2 metalu.net 2020"
- board text removed: "+8V"
- board text removed: "ServoRelais v1"
